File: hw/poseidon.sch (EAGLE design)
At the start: 162 parts, among them IC1 MCP1703DB, J1 DCJ0202, Q1 IRF512, Q10 IRF512, Q11 IRF512, Q12 IRF512, Q13 IRF512, Q14 IRF512, Q15 IRF512, Q16 IRF512, Q17 IRF512, Q18 IRF512, Q19 IRF512, Q2 IRF512, Q3 IRF512, Q4 IRF512, Q5 IRF512, Q6 IRF512, Q7 IRF512, Q8 IRF512, Q9 IRF512, T1 2N5088, T10 2N5088, T11 2N5088, T12 2N5088, T13 2N5088, T14 2N5088, T15 2N5088, T16 2N5088, T2 2N5088, T3 2N5088, T4 2N5088, T5 2N5088, T6 2N5088, T7 2N5088, T8 2N5088, T9 2N5088, X1 B4B-ZR, X2 1296-T10, X3 22-23-2041, X4 22-23-2041, X5 22-23-2021

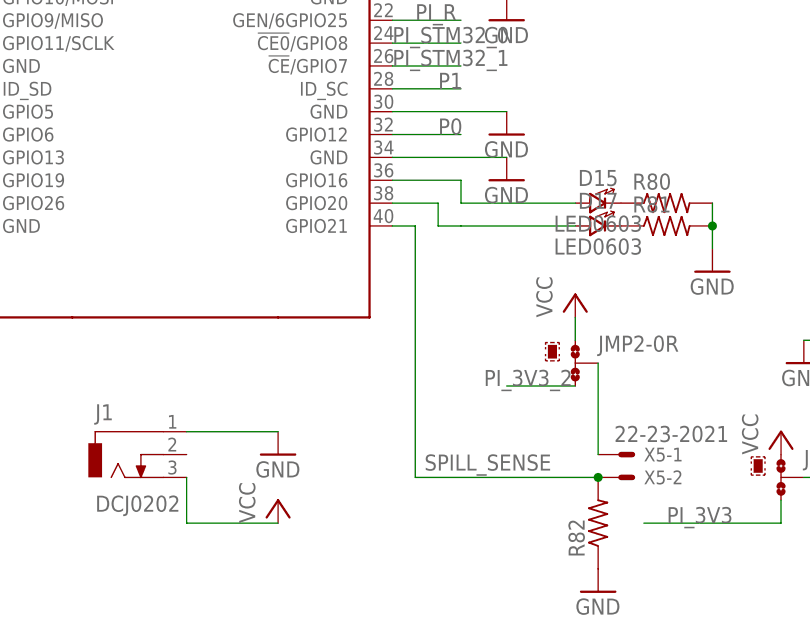
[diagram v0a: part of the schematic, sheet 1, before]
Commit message: Fixed problems with first revision, including barrel jack polarity
Also tidied up labels, connected extra vias to ground, created
test points for power rails. Still need to fix water level sensor
connector, which is currently too small.
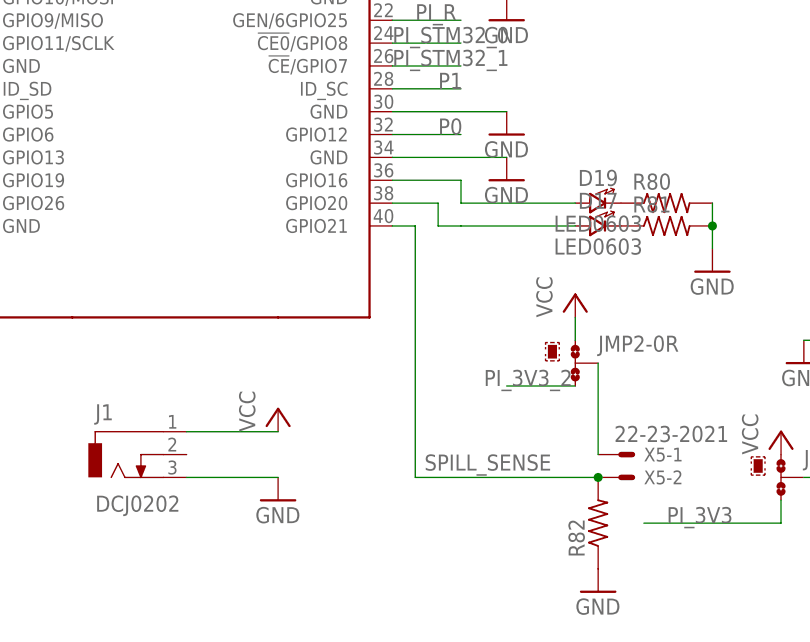
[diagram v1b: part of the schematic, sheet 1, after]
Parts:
- removed THERM_D15: CREE-XT-E-WHITE, leds:CREE-XT-E-WHITE
- added D19: LED0603, leds:LED0603
- D15: value LED0603 -> CREE-XT-E-WHITE; device leds:LED0603 -> leds:CREE-XT-E-WHITE
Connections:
- net GND: now also J1.3; no longer J1.1
- net N$26: now also D19.ANODE; no longer D15.ANODE
- net N$5: now also D19.CATHODE; no longer D15.CATHODE
- net N$59: now also D15G$1.CATHODE; no longer THERM_D15G$1.CATHODE
- net THERM_D15: now also D15G$2.P$1; no longer THERM_D15G$2.P$1
- net VCC: now also D15G$1.ANODE, J1.1; no longer J1.3, THERM_D15G$1.ANODE
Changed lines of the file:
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@@
 <part name="Q15" library="transistor-power" library_urn="urn:adsk.eagle:library:400" deviceset="IRF512" device="" package3d_urn="urn:adsk.eagle:package:29484/3"/>
 <part name="R43" library="rcl" library_urn="urn:adsk.eagle:library:334" deviceset="R-US_" device="R0805" package3d_urn="urn:adsk.eagle:package:23553/2" value="10k"/>
-<part name="THERM_D15" library="leds" deviceset="CREE-XT-E" device="-WHITE"/>
+<part name="D15" library="leds" deviceset="CREE-XT-E" device="-WHITE"/>
 <part name="P+29" library="supply1" library_urn="urn:adsk.eagle:library:371" deviceset="VCC" device=""/>
 <part name="GND29" library="supply1" library_urn="urn:adsk.eagle:library:371" deviceset="GND" device=""/>
@@
 <part name="R78" library="resistor" library_urn="urn:adsk.eagle:library:348" deviceset="R-US_" device="R0805" package3d_urn="urn:adsk.eagle:package:23553/2"/>
 <part name="R79" library="resistor" library_urn="urn:adsk.eagle:library:348" deviceset="R-US_" device="R0805" package3d_urn="urn:adsk.eagle:package:23553/2"/>
-<part name="D15" library="leds" deviceset="LED" device="0603"/>
+<part name="D19" library="leds" deviceset="LED" device="0603"/>
 <part name="D17" library="leds" deviceset="LED" device="0603"/>
 <part name="R80" library="resistor" library_urn="urn:adsk.eagle:library:348" deviceset="R-US_" device="R0805" package3d_urn="urn:adsk.eagle:package:23553/2"/>
@@
 <attribute name="VALUE" x="50.8" y="6.35" size="1.778" layer="96"/>
 </instance>
-<instance part="GND45" gate="1" x="71.12" y="12.7" smashed="yes">
-<attribute name="VALUE" x="68.58" y="10.16" size="1.778" layer="96"/>
-</instance>
-<instance part="P+4" gate="VCC" x="71.12" y="7.62" smashed="yes">
-<attribute name="VALUE" x="68.58" y="5.08" size="1.778" layer="96" rot="R90"/>
+<instance part="GND45" gate="1" x="71.12" y="7.62" smashed="yes">
+<attribute name="VALUE" x="68.58" y="5.08" size="1.778" layer="96"/>
+</instance>
+<instance part="P+4" gate="VCC" x="71.12" y="17.78" smashed="yes">
+<attribute name="VALUE" x="68.58" y="15.24" size="1.778" layer="96" rot="R90"/>
 </instance>
 <instance part="U$21" gate="G$1" x="154.94" y="40.64" smashed="yes"/>
@@
 </instance>
 <instance part="JMP2" gate="G$2" x="101.6" y="25.4" smashed="yes"/>
-<instance part="D15" gate="G$1" x="106.68" y="40.64" smashed="yes">
+<instance part="D19" gate="G$1" x="106.68" y="40.64" smashed="yes">
 <attribute name="NAME" x="106.68" y="42.545" size="1.778" layer="95" ratio="12" align="bottom-center"/>
 <attribute name="VALUE" x="106.68" y="37.465" size="1.778" layer="96" ratio="12" align="bottom-center"/>
@@
 <segment>
 <pinref part="P+4" gate="VCC" pin="VCC"/>
-<pinref part="J1" gate="G$1" pin="3"/>
-<wire x1="71.12" y1="5.08" x2="60.96" y2="5.08" width="0.1524" layer="91"/>
-<wire x1="60.96" y1="5.08" x2="60.96" y2="10.16" width="0.1524" layer="91"/>
+<wire x1="71.12" y1="15.24" x2="60.96" y2="15.24" width="0.1524" layer="91"/>
+<pinref part="J1" gate="G$1" pin="1"/>
 </segment>
 <segment>
@@
 <pinref part="U$1" gate="G$1" pin="GND@1"/>
 <wire x1="15.24" y1="76.2" x2="35.56" y2="76.2" width="0.1524" layer="91"/>
-</segment>
-<segment>
-<pinref part="J1" gate="G$1" pin="1"/>
-<pinref part="GND45" gate="1" pin="GND"/>
-<wire x1="60.96" y1="15.24" x2="71.12" y2="15.24" width="0.1524" layer="91"/>
 </segment>
 <segment>
@@
 <pinref part="R82" gate="G$1" pin="1"/>
 <pinref part="GND57" gate="1" pin="GND"/>
+</segment>
+<segment>
+<pinref part="J1" gate="G$1" pin="3"/>
+<pinref part="GND45" gate="1" pin="GND"/>
+<wire x1="71.12" y1="10.16" x2="60.96" y2="10.16" width="0.1524" layer="91"/>
 </segment>
 </net>
@@
 <net name="N$5" class="0">
 <segment>
-<pinref part="D15" gate="G$1" pin="CATHODE"/>
+<pinref part="D19" gate="G$1" pin="CATHODE"/>
 <pinref part="R80" gate="G$1" pin="1"/>
 </segment>
@@
 <net name="N$26" class="0">
 <segment>
-<pinref part="D15" gate="G$1" pin="ANODE"/>
+<pinref part="D19" gate="G$1" pin="ANODE"/>
 <wire x1="104.14" y1="40.64" x2="91.44" y2="40.64" width="0.1524" layer="91"/>
 <wire x1="91.44" y1="40.64" x2="91.44" y2="43.18" width="0.1524" layer="91"/>
@@
 <attribute name="VALUE" x="18.542" y="41.91" size="1.778" layer="96" rot="R90"/>
 </instance>
-<instance part="THERM_D15" gate="G$1" x="25.4" y="48.26" smashed="yes" rot="R270">
+<instance part="D15" gate="G$1" x="25.4" y="48.26" smashed="yes" rot="R270">
 <attribute name="NAME" x="28.739009375" y="52.7812" size="1.778" layer="95" ratio="12" rot="R180" align="bottom-center"/>
 <attribute name="VALUE" x="38.419121875" y="45.5168" size="1.778" layer="96" ratio="12" rot="R180" align="bottom-center"/>
@@
 <instance part="D13" gate="G$2" x="187.96" y="27.94" smashed="yes"/>
 <instance part="D14" gate="G$2" x="187.96" y="20.32" smashed="yes"/>
-<instance part="THERM_D15" gate="G$2" x="187.96" y="12.7" smashed="yes"/>
+<instance part="D15" gate="G$2" x="187.96" y="12.7" smashed="yes"/>
 <instance part="D16" gate="G$2" x="187.96" y="5.08" smashed="yes"/>
 <instance part="+3V1" gate="G$1" x="-73.66" y="-76.2" smashed="yes">
@@
 <pinref part="R43" gate="G$1" pin="2"/>
 <wire x1="15.24" y1="50.8" x2="15.24" y2="53.34" width="0.1524" layer="91"/>
-<pinref part="THERM_D15" gate="G$1" pin="ANODE"/>
+<pinref part="D15" gate="G$1" pin="ANODE"/>
 <wire x1="15.24" y1="53.34" x2="20.32" y2="53.34" width="0.1524" layer="91"/>
 <wire x1="20.32" y1="53.34" x2="25.4" y2="53.34" width="0.1524" layer="91"/>
@@
 <segment>
 <pinref part="Q15" gate="1" pin="D"/>
-<pinref part="THERM_D15" gate="G$1" pin="CATHODE"/>
+<pinref part="D15" gate="G$1" pin="CATHODE"/>
 <wire x1="25.4" y1="43.18" x2="25.4" y2="45.72" width="0.1524" layer="91"/>
 </segment>
@@
 <net name="THERM_D15" class="0">
 <segment>
-<pinref part="THERM_D15" gate="G$2" pin="P$1"/>
+<pinref part="D15" gate="G$2" pin="P$1"/>
 <wire x1="193.04" y1="12.7" x2="200.66" y2="12.7" width="0.1524" layer="91"/>
 <label x="190.5" y="10.16" size="1.778" layer="95"/>
